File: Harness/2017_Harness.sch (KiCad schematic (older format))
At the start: 8 parts

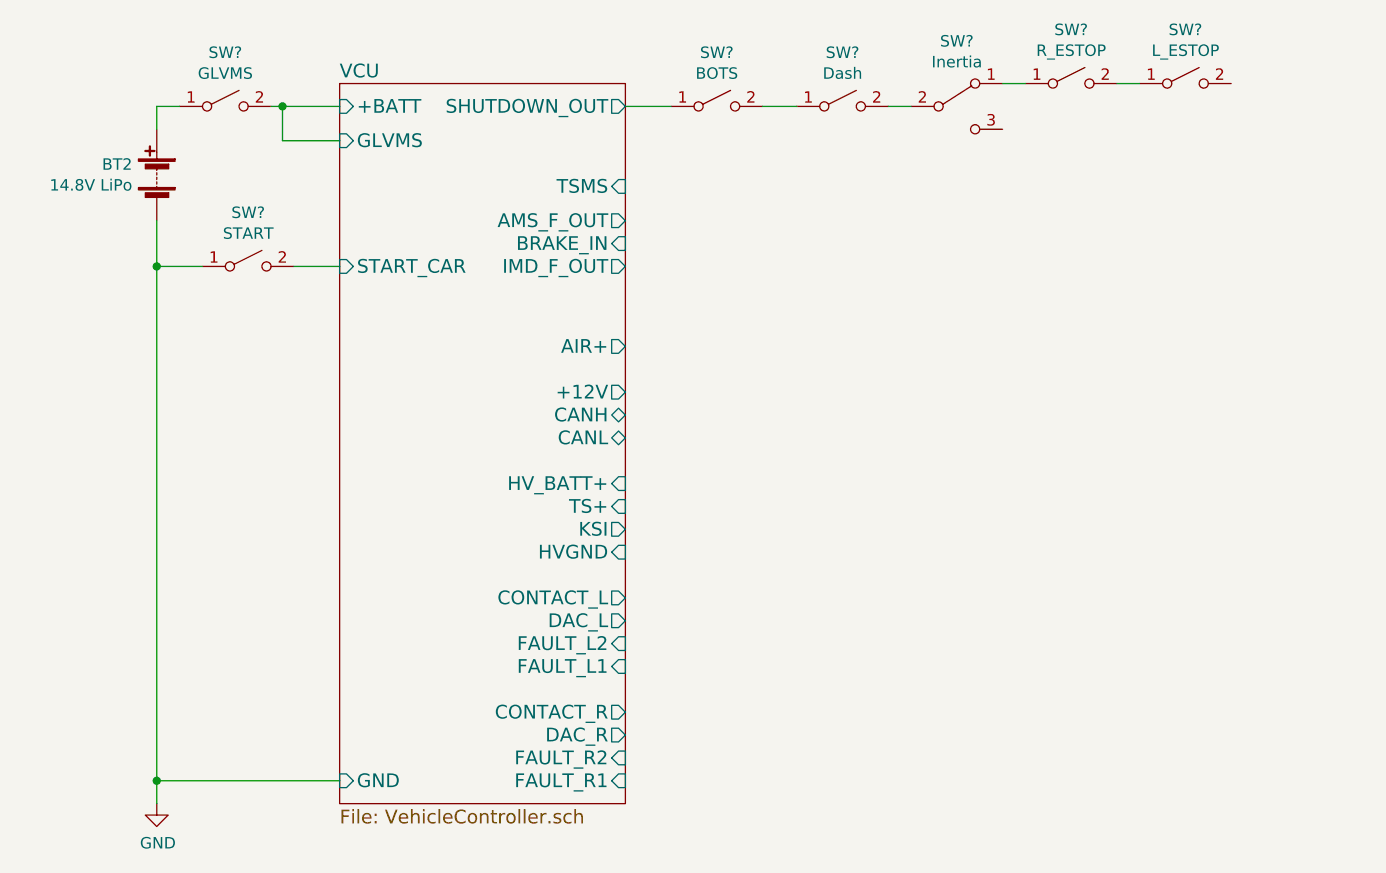
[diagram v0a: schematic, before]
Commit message: Fleshed out harness diagram
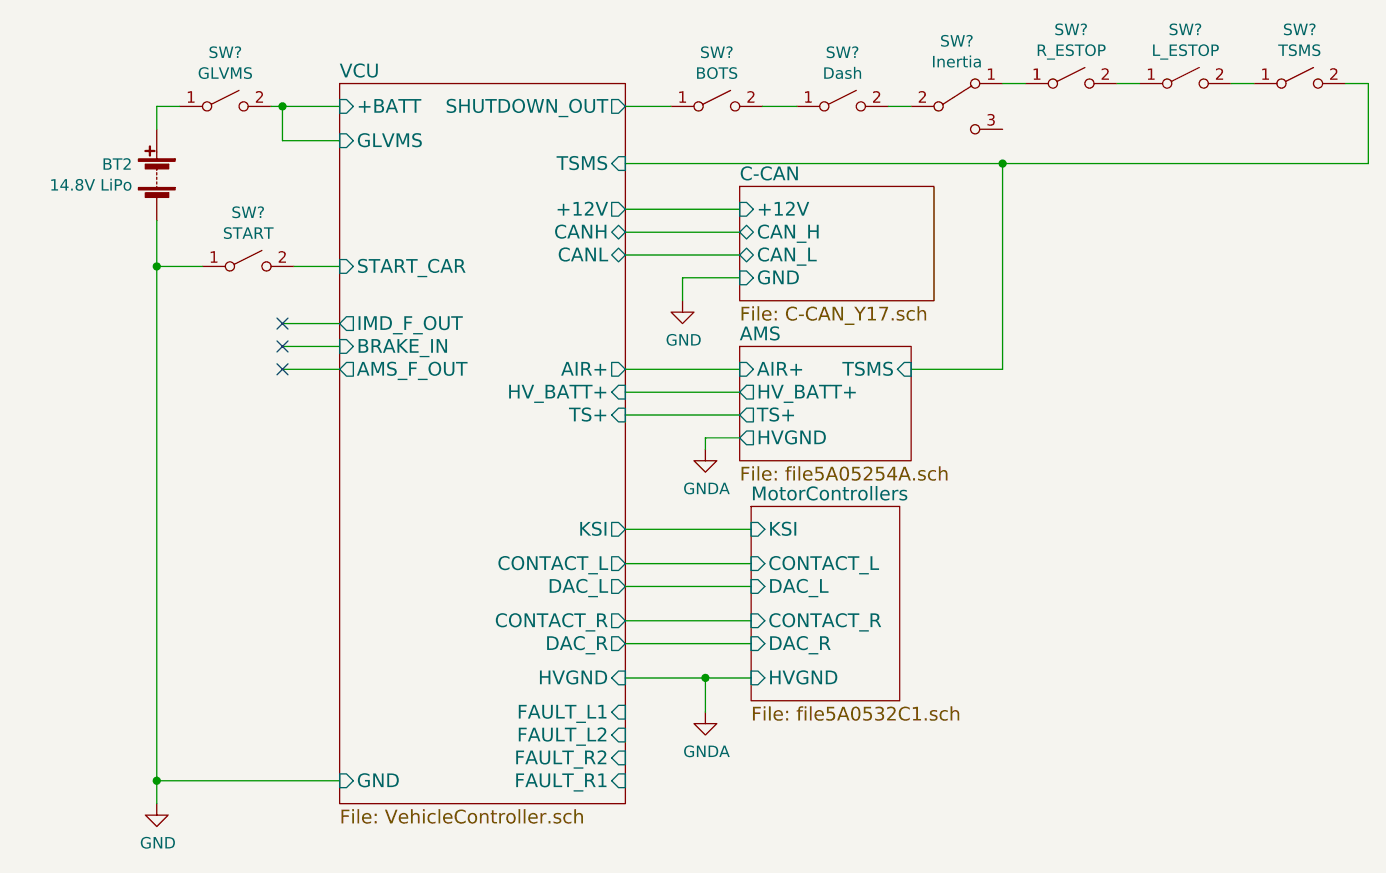
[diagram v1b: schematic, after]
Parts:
- added SW?: TSMS, symbol SW_SPST
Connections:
- net at SW?.2 (B): now also SW?.1 (A)
- new net AMS/TSMS: SW?.2 (B)
- no-connect marks 0 -> 3
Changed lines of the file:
@@
 $Descr A4 11693 8268
 encoding utf-8
-Sheet 1 6
+Sheet 1 9
 Title ""
 Date "2017-11-07"
@@
 F0 "VCU" 60
 F1 "VehicleController.sch" 60
-F2 "IMD_F_OUT" O R 3750 2300 60
+F2 "IMD_F_OUT" O L 2500 2550 60
 F3 "SHUTDOWN_OUT" O R 3750 1600 60
 F4 "START_CAR" I L 2500 2300 60
-F5 "TSMS" I R 3750 1950 60
+F5 "TSMS" I R 3750 1850 60
 F6 "GLVMS" I L 2500 1750 60
-F7 "AMS_F_OUT" O R 3750 2100 60
-F8 "BRAKE_IN" I R 3750 2200 60
-F9 "AIR+" O R 3750 2650 60
+F7 "AMS_F_OUT" O L 2500 2750 60
+F8 "BRAKE_IN" I L 2500 2650 60
+F9 "AIR+" O R 3750 2750 60
 F10 "+BATT" I L 2500 1600 60
 F11 "GND" I L 2500 4550 60
-F12 "+12V" O R 3750 2850 60
-F13 "CANH" B R 3750 2950 60
-F14 "CANL" B R 3750 3050 60
-F15 "HV_BATT+" I R 3750 3250 60
-F16 "TS+" I R 3750 3350 60
-F17 "HVGND" I R 3750 3550 60
+F12 "+12V" O R 3750 2050 60
+F13 "CANH" B R 3750 2150 60
+F14 "CANL" B R 3750 2250 60
+F15 "HV_BATT+" I R 3750 2850 60
+F16 "TS+" I R 3750 2950 60
+F17 "HVGND" I R 3750 4100 60
 F18 "KSI" O R 3750 3450 60
-F19 "CONTACT_L" O R 3750 3750 60
-F20 "DAC_L" O R 3750 3850 60
-F21 "FAULT_L2" I R 3750 3950 60
-F22 "FAULT_L1" I R 3750 4050 60
-F23 "CONTACT_R" O R 3750 4250 60
-F24 "DAC_R" O R 3750 4350 60
+F19 "CONTACT_L" O R 3750 3600 60
+F20 "DAC_L" O R 3750 3700 60
+F21 "FAULT_L2" I R 3750 4350 60
+F22 "FAULT_L1" I R 3750 4250 60
+F23 "CONTACT_R" O R 3750 3850 60
+F24 "DAC_R" O R 3750 3950 60
 F25 "FAULT_R2" I R 3750 4450 60
 F26 "FAULT_R1" I R 3750 4550 60
@@
 $EndComp
 Wire Wire Line
-	1700 2100 1700 4650
+	1700 2100 1700 2300
+Wire Wire Line
+	1700 2300 1700 4550
+Wire Wire Line
+	1700 4550 1700 4650
 Wire Wire Line
 	1700 1700 1700 1600
@@
 	1700 1600 1800 1600
 Wire Wire Line
-	2200 1600 2500 1600
+	2200 1600 2250 1600
+Wire Wire Line
+	2250 1600 2500 1600
 Wire Wire Line
 	2500 1750 2250 1750
@@
 	2500 4550 1700 4550
 Connection ~ 1700 4550
+$Comp
+L SW_SPST SW?
+U 1 1 5A051764
+P 6700 1500
+F 0 "SW?" H 6700 1735 50  0000 C CNN
+F 1 "TSMS" H 6700 1644 50  0000 C CNN
+F 2 "" H 6700 1500 50  0001 C CNN
+F 3 "" H 6700 1500 50  0001 C CNN
+	1    6700 1500
+	1    0    0    -1
+$EndComp
+Wire Wire Line
+	6500 1500 6400 1500
+Wire Wire Line
+	3750 1850 5400 1850
+Wire Wire Line
+	5400 1850 7000 1850
+Wire Wire Line
+	7000 1850 7000 1500
+Wire Wire Line
+	7000 1500 6900 1500
+$Sheet
+S 4250 2650 750  500
+U 5A05254B
+F0 "AMS" 60
+F1 "file5A05254A.sch" 60
+F2 "AIR+" I L 4250 2750 60
+F3 "HV_BATT+" O L 4250 2850 60
+F4 "TS+" O L 4250 2950 60
+F5 "HVGND" O L 4250 3050 60
+F6 "TSMS" I R 5000 2750 60
+$EndSheet
+$Sheet
+S 4300 3350 650  850
+U 5A0532C2
+F0 "MotorControllers" 60
+F1 "file5A0532C1.sch" 60
+F2 "KSI" I L 4300 3450 60
+F3 "CONTACT_L" I L 4300 3600 60
+F4 "DAC_L" I L 4300 3700 60
+F5 "CONTACT_R" I L 4300 3850 60
+F6 "DAC_R" I L 4300 3950 60
+F7 "HVGND" I L 4300 4100 60
+$EndSheet
+Wire Wire Line
+	4300 3450 3750 3450
+Wire Wire Line
+	3750 3600 4300 3600
+Wire Wire Line
+	4300 3700 3750 3700
+Wire Wire Line
+	3750 3850 4300 3850
+Wire Wire Line
+	4300 3950 3750 3950
+Wire Wire Line
+	3750 4100 4100 4100
+Wire Wire Line
+	4100 4100 4300 4100
+Wire Wire Line
+	2500 2550 2250 2550
+NoConn ~ 2250 2550
+NoConn ~ 2250 2650
+NoConn ~ 2250 2750
+Wire Wire Line
+	2250 2650 2500 2650
+Wire Wire Line
+	2250 2750 2500 2750
+Wire Wire Line
+	4250 3050 4100 3050
+Connection ~ 4100 4100
+Wire Wire Line
+	3750 2950 4250 2950
+Wire Wire Line
+	4250 2850 3750 2850
+Wire Wire Line
+	3750 2750 4250 2750
+$Comp
+L GNDA #PWR?
+U 1 1 5A05F289
+P 4100 3100
+F 0 "#PWR?" H 4100 2850 50  0001 C CNN
+F 1 "GNDA" H 4105 2927 50  0000 C CNN
+F 2 "" H 4100 3100 50  0001 C CNN
+F 3 "" H 4100 3100 50  0001 C CNN
+	1    4100 3100
+	1    0    0    -1
+$EndComp
+Wire Wire Line
+	4100 3050 4100 3100
+$Comp
+L GNDA #PWR?
+U 1 1 5A05F650
+P 4100 4250
+F 0 "#PWR?" H 4100 4000 50  0001 C CNN
+F 1 "GNDA" H 4105 4077 50  0000 C CNN
+F 2 "" H 4100 4250 50  0001 C CNN
+F 3 "" H 4100 4250 50  0001 C CNN
+	1    4100 4250
+	1    0    0    -1
+$EndComp
+Wire Wire Line
+	4100 4250 4100 4100
+Wire Wire Line
+	5000 2750 5400 2750
+Wire Wire Line
+	5400 2750 5400 1850
+Connection ~ 5400 1850
+$Sheet
+S 4250 1950 850  500
+U 5A051AEE
+F0 "C-CAN" 60
+F1 "C-CAN_Y17.sch" 60
+F2 "+12V" I L 4250 2050 60
+F3 "CAN_H" B L 4250 2150 60
+F4 "GND" I L 4250 2350 60
+F5 "CAN_L" B L 4250 2250 60
+$EndSheet
+Wire Wire Line
+	3750 2050 4250 2050
+Wire Wire Line
+	4250 2150 3750 2150
+Wire Wire Line
+	3750 2250 4250 2250
+$Comp
+L GND #PWR?
+U 1 1 5A05571C
+P 4000 2450
+F 0 "#PWR?" H 4000 2200 50  0001 C CNN
+F 1 "GND" H 4005 2277 50  0000 C CNN
+F 2 "" H 4000 2450 50  0001 C CNN
+F 3 "" H 4000 2450 50  0001 C CNN
+	1    4000 2450
+	1    0    0    -1
+$EndComp
+Wire Wire Line
+	4250 2350 4000 2350
+Wire Wire Line
+	4000 2350 4000 2450
 $EndSCHEMATC
